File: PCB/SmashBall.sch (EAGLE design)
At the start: 7 parts

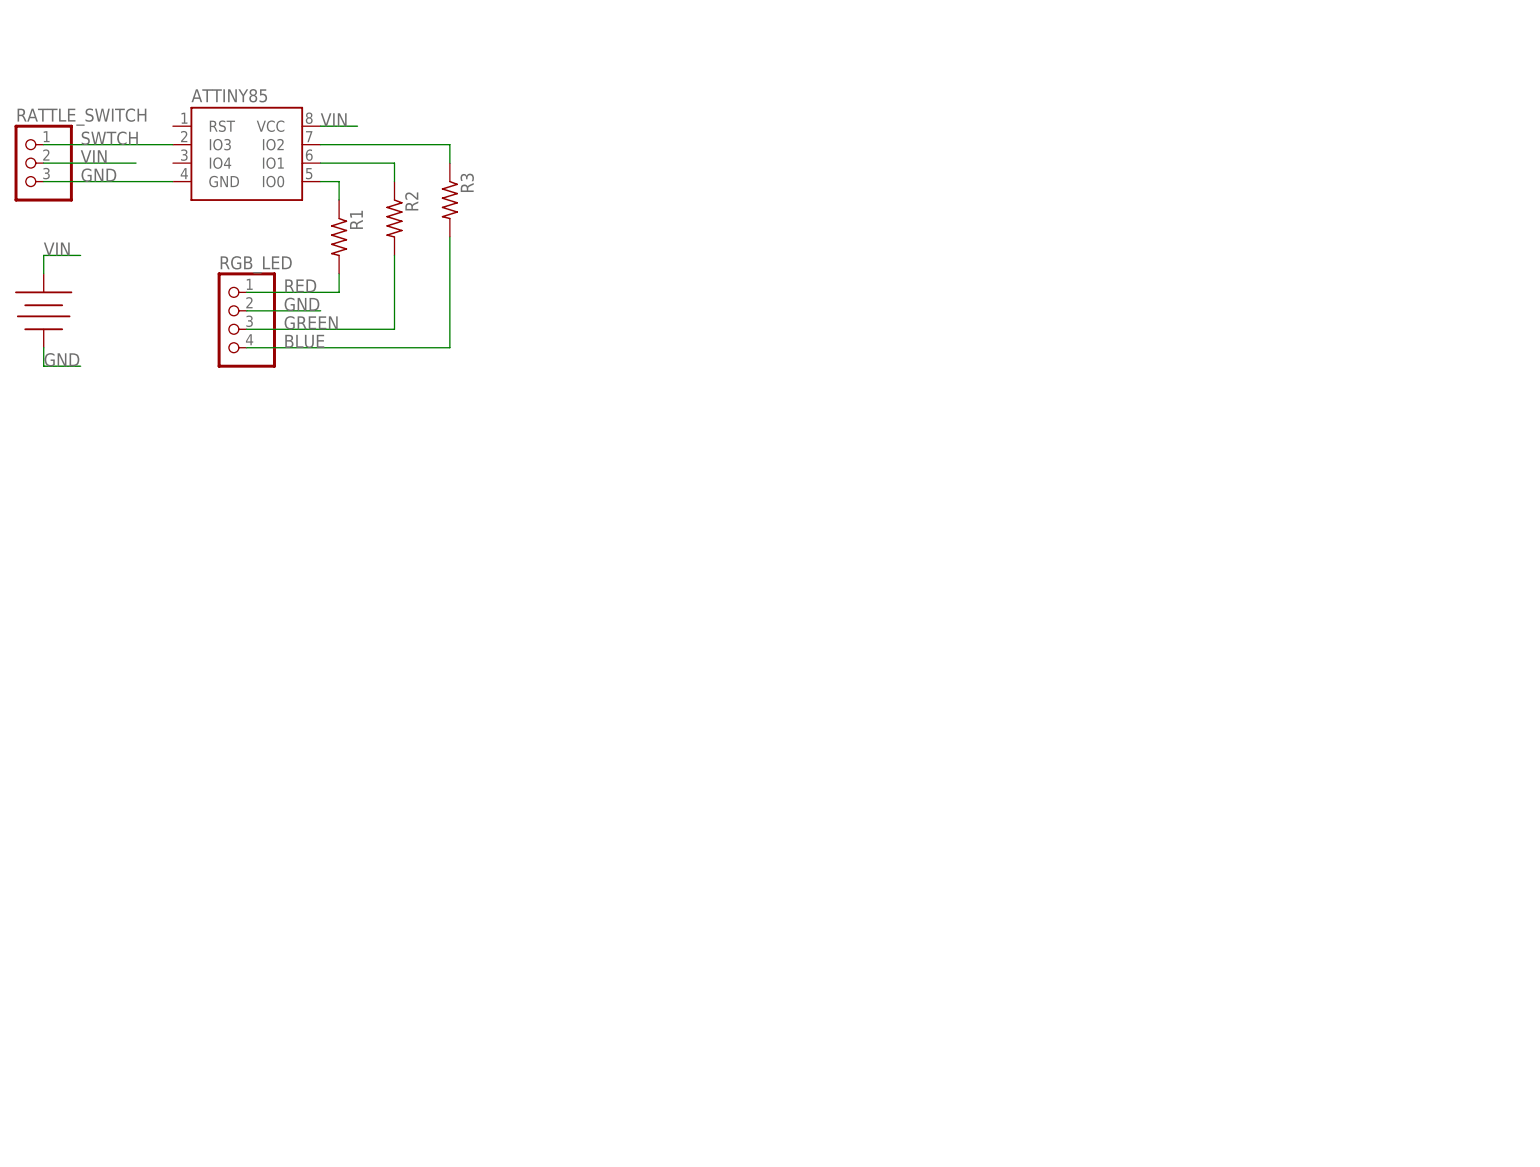
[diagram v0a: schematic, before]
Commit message: Redid the schematic and am halfway through redoing the board design.
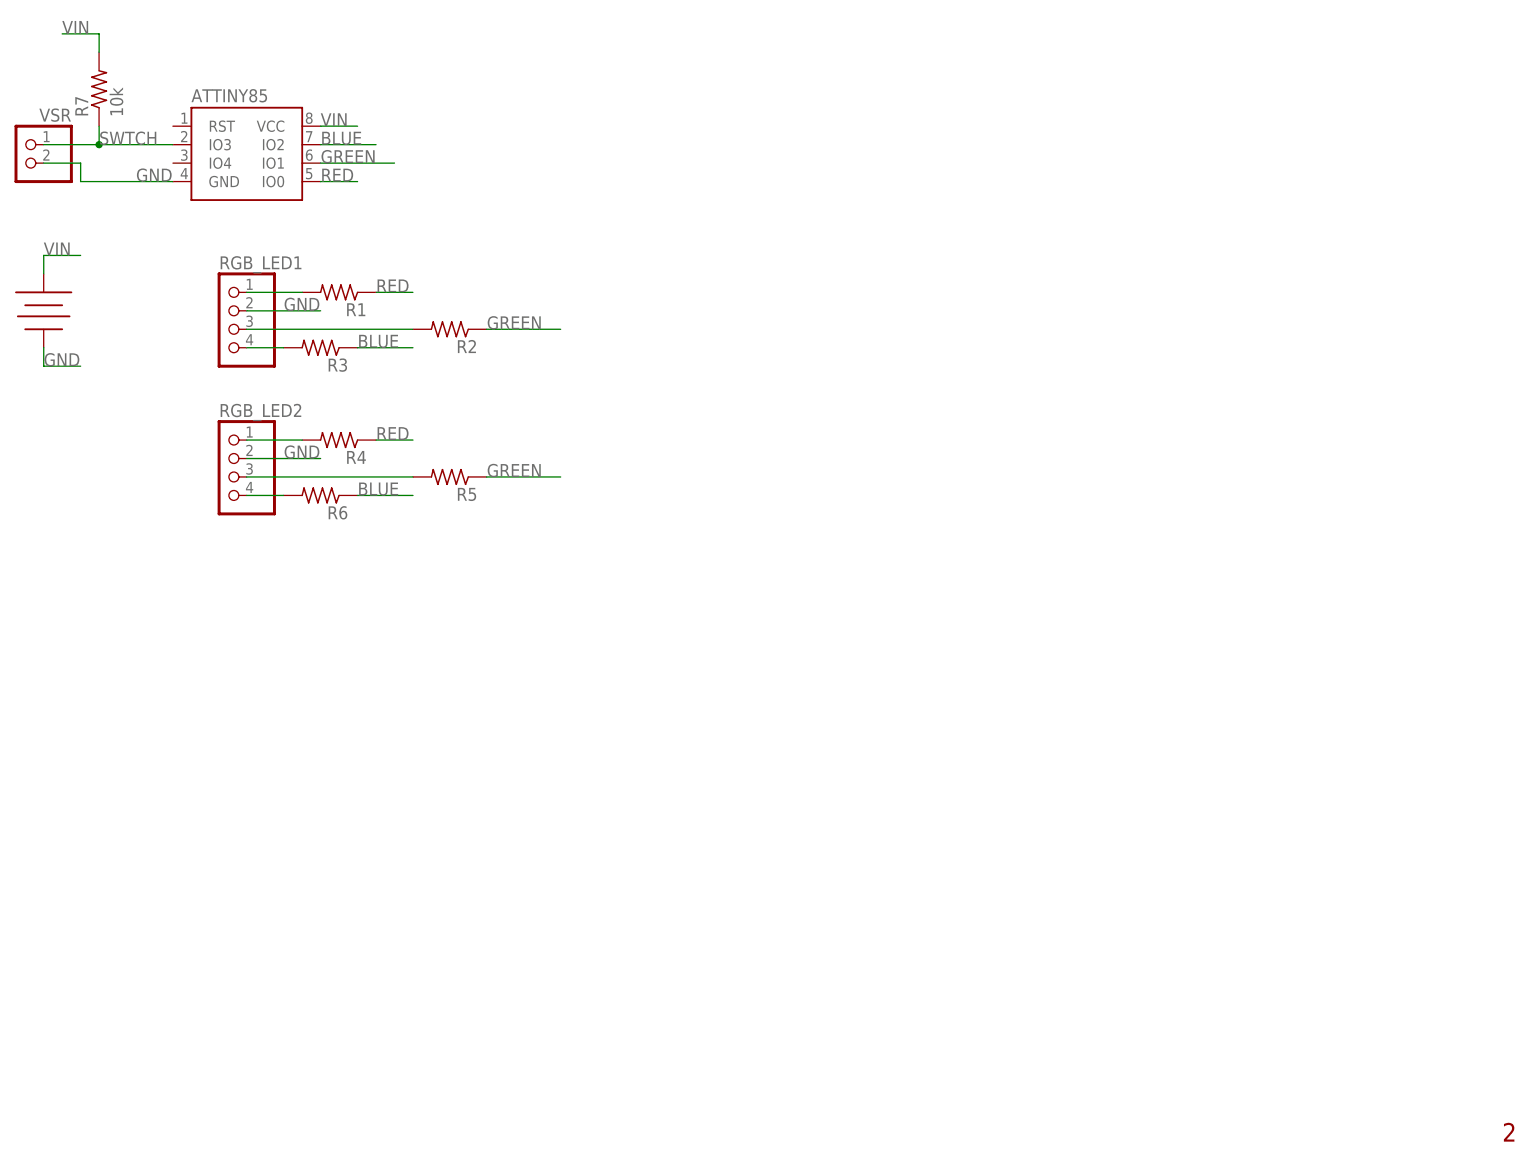
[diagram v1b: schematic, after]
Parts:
- removed RATTLE_SWITCH: (no value), pinhead:PINHD-1X3
- added R4, R5, R6: (no value), rcl:R-US_0207/2V
- added R7: 10k, rcl:R-US_0207/2V
- added RGB_LED2: (no value), pinhead:PINHD-1X4
- added VSR: (no value), pinhead:PINHD-1X2
- renumbered RGB_LED to RGB_LED1
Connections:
- removed net N$1: R1.1, U$1.IO0
- removed net N$2: R2.1, U$1.IO1
- removed net N$3: R3.1, U$1.IO2
- new net BLUE1: R3.2, RGB_LED1.4
- new net BLUE2: R6.2, RGB_LED2.4
- new net GREEN1: R2.2, RGB_LED1.3
- new net GREEN2: R5.2, RGB_LED2.3
- new net RED1: R1.2, RGB_LED1.1
- new net RED2: R4.2, RGB_LED2.1
- net BLUE: now also R3.1, R6.1, U$1.IO2; no longer R3.2, RGB_LED1.4
- net GND: now also RGB_LED2.2, VSR.2; no longer RATTLE_SWITCH.3
- net GREEN: now also R2.1, R5.1, U$1.IO1; no longer R2.2, RGB_LED1.3
- net RED: now also R1.1, R4.1, U$1.IO0; no longer R1.2, RGB_LED1.1
- net SWTCH: now also R7.1, VSR.1; no longer RATTLE_SWITCH.1
- net VIN: now also R7.2; no longer RATTLE_SWITCH.2
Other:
- note added: "2"
- moved on the sheet: R1, R2, R3
